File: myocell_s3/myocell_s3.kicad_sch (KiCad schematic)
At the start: 6 parts, among them J1 Conn_01x08, J2 Conn_01x08, J3 Conn_01x08, J4 Conn_01x08, J5 Battery Connector JC2, J6 USB_B_Micro

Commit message: recovery commit
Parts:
- removed J6: USB_B_Micro, Connector_USB:USB_Micro-B_Molex_47346-0001, symbol Connector:USB_B_Micro
- added J7: USB_C_Receptacle_USB2.0_16P, Connector_USB:USB_C_Receptacle_GCT_USB4110, symbol Connector:USB_C_Receptacle_USB2.0_16P
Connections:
- new net: J7.A1 (GND), J7.A12 (GND), J7.B1 (GND), J7.B12 (GND)
- new net: J7.A4 (VBUS), J7.A9 (VBUS), J7.B4 (VBUS), J7.B9 (VBUS)
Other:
- sheet cpu_wroom_esp32 ports: added none; removed EN

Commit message: working on schematic
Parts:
- added R14, R15: 5.1k, Resistor_SMD:R_0805_2012Metric_Pad1.20x1.40mm_HandSolder, symbol Device:R_US
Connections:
- net GND: now also R14.1, R15.1
- net power_supply/VUSB/2.1A: now also J7.A4 (VBUS), J7.A9 (VBUS), J7.B4 (VBUS), J7.B9 (VBUS)
- net at J7.A5 (CC1): now also R15.2
- net cpu_wroom_esp32/D+: now reaches J7.A6 (D+)
- net cpu_wroom_esp32/D+: now also J7.B6 (D+)
- net cpu_wroom_esp32/D-: now reaches J7.A7 (D-)
- net cpu_wroom_esp32/D-: now also J7.B7 (D-)
- net at J7.B5 (CC2): now also R14.2
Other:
- removed sheet usb
- sheet adc_8 ports: added RLD; removed adcVref, rld_Out
- sheet cpu_wroom_esp32 ports: added D+, D-; removed IO0, RXD0, TXD0
- moved on the sheet: J7

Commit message: working on schematic
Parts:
- added C55, C56: 10pF, Capacitor_SMD:C_0805_2012Metric_Pad1.18x1.45mm_HandSolder, symbol Device:C
- added R30, R31: 20, Resistor_SMD:R_0805_2012Metric_Pad1.20x1.40mm_HandSolder, symbol Device:R_US
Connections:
- net GND: now also C55.1, C56.2
- net cpu_wroom_esp32/D+: now also R30.1; no longer J7.A6 (D+), J7.B6 (D+)
- net cpu_wroom_esp32/D-: now also R31.1; no longer J7.A7 (D-), J7.B7 (D-)
- new net: C55.2, J7.A6 (D+), J7.B6 (D+), R30.2
- new net: C56.1, J7.A7 (D-), J7.B7 (D-), R31.2
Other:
- sheet cpu_wroom_esp32 ports: added clk, fspi_clk, fspi_cs0, fspi_miso, fspi_mosi, pwdn, reset, start; removed gpio18_vspi_sck, gpio19_vspi_miso, gpio21_start, gpio22_pwdn, gpio23_vspi_mosi, gpio27, gpio32, gpio33, gpio4, gpio5_vspi_ss
- note added: "esp32-s3 is spi master miso - master in, slave out mosi - master out, slave in"

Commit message: working on schematic transfer
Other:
- sheet cpu_wroom_esp32 ports: added bat_mon; removed none
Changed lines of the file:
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@@
 	(wire
 		(pts
+			(xy 151.13 101.6) (xy 189.23 101.6)
+		)
+		(stroke
+			(width 0)
+			(type default)
+		)
+	)
+	(wire
+		(pts
 			(xy 114.3 39.37) (xy 114.3 43.18)
 		)
@@
 	(wire
 		(pts
-			(xy 160.02 101.6) (xy 189.23 101.6)
-		)
-		(stroke
-			(width 0)
-			(type default)
-		)
-	)
-	(wire
-		(pts
 			(xy 86.36 62.23) (xy 90.17 62.23)
 		)
@@
 	(wire
 		(pts
+			(xy 151.13 101.6) (xy 151.13 72.39)
+		)
+		(stroke
+			(width 0)
+			(type default)
+		)
+	)
+	(wire
+		(pts
 			(xy 125.73 54.61) (xy 138.43 54.61)
 		)
@@
 			(effects
 				(font
+					(size 1.27 1.27)
+				)
+				(justify left)
+			)
+		)
+		(pin "bat_mon" input
+			(at 151.13 72.39 270)
+			(effects
+				(font

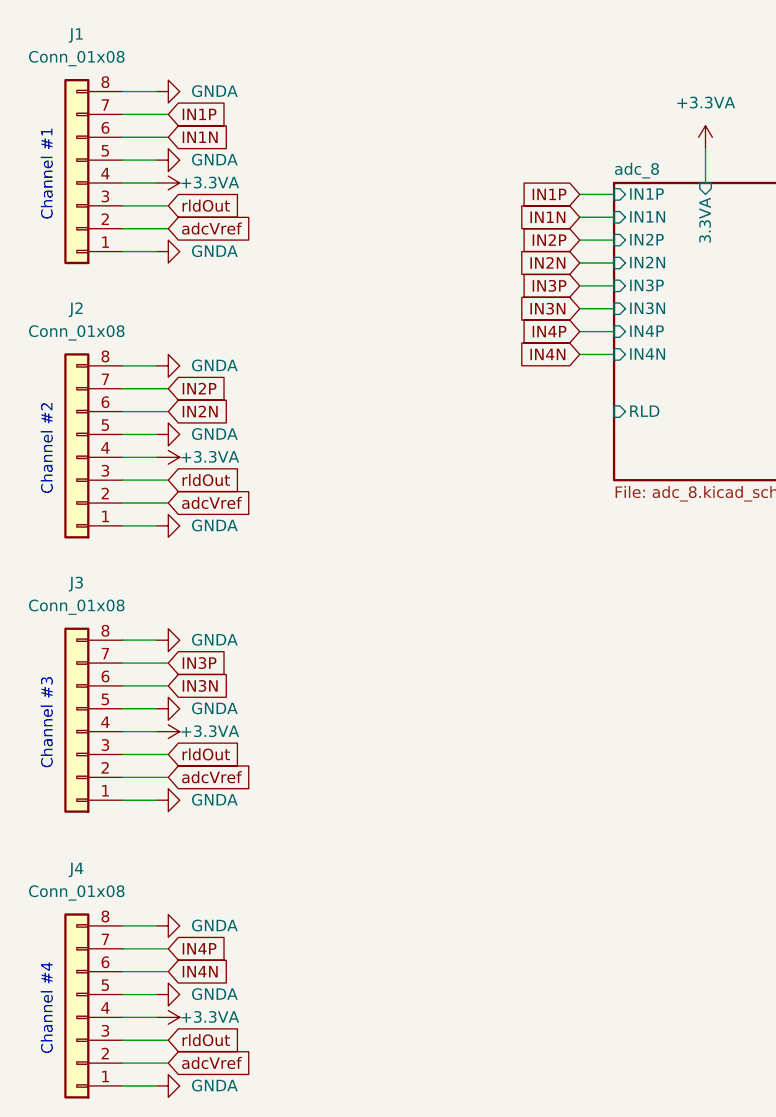
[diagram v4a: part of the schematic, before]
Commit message: RLDINV still unconnected
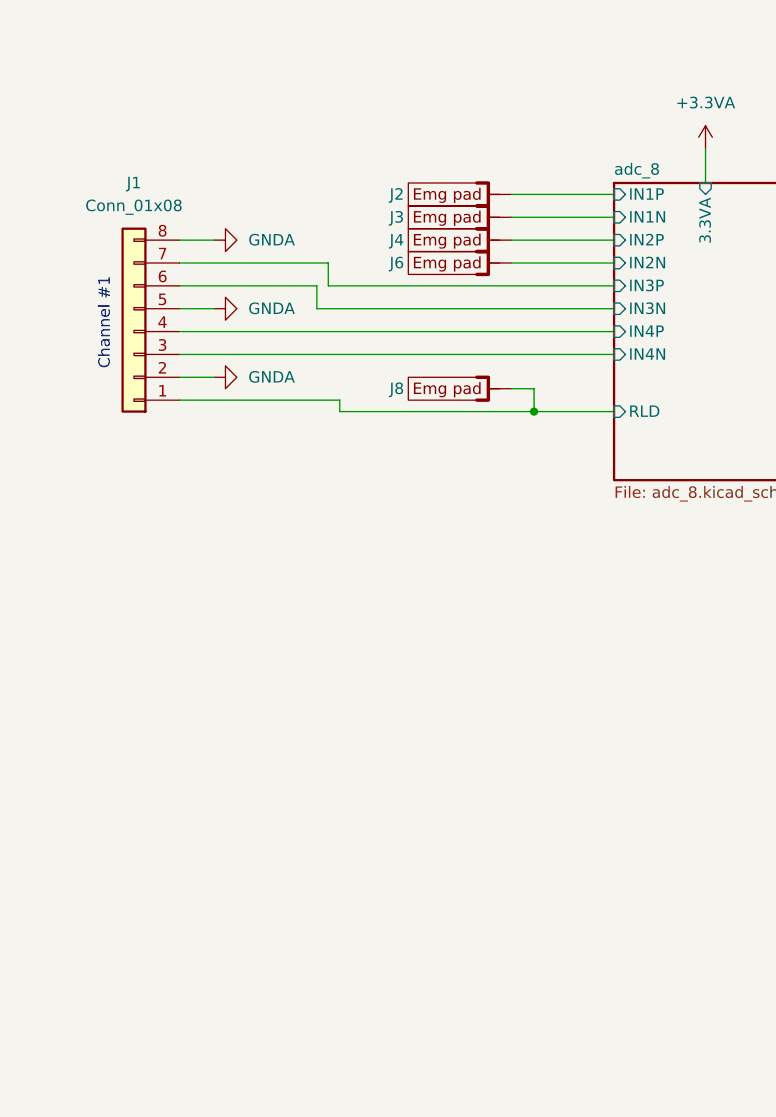
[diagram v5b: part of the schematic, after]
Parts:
- removed J2, J3, J4: Conn_01x08, Connector_FFC-FPC:Hirose_FH12-8S-0.5SH_1x08-1MP_P0.50mm_Horizontal, symbol Connector_Generic:Conn_01x08
- added J2, J3: (no value), emg:EMG_PAD_10_7, symbol myocell_s3:emg_pad
- added J4, J6, J8: ~, emg:EMG_PAD_10_7, symbol myocell_s3:emg_pad
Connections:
- net adcVref is gone; now on net GNDA: J1.2 (Pin_2)
- net +3.3VA: no longer J1.4 (Pin_4)
- net GNDA: no longer J1.1 (Pin_1)
- net adc_8/RLD: now also J1.1 (Pin_1), J8.1
- net IN1N renamed adc_8/IN3N
- net IN1P renamed adc_8/IN3P
- net rldOut renamed adc_8/IN4N
- new net adc_8/IN1N: J3.1
- new net adc_8/IN1P: J2.1
- new net adc_8/IN2N: J6.1
- new net adc_8/IN2P: J4.1
- new net adc_8/IN4P: J1.4 (Pin_4)
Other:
- note removed: "Channel #2"
- note removed: "Channel #3"
- note removed: "Channel #4"
- moved on the sheet: J1

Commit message: MSS22D18 slider switch added
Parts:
- J2, J3: value (none) -> ~
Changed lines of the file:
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@@
 			)
 		)
-		(property "Value" ""
+		(property "Value" "~"
 			(at 72.39 40.64 0)
 			(effects
@@
 			)
 		)
-		(property "Value" ""
+		(property "Value" "~"
 			(at 72.39 43.18 0)
 			(effects

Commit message: schematic and footprints done
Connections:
- net +3.3VA: now also J1.5 (Pin_5)
- net GNDA: no longer J1.5 (Pin_5)
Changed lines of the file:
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@@
+	(wire
+		(pts
+			(xy 41.91 57.15) (xy 44.45 57.15)
+		)
+		(stroke
+			(width 0)
+			(type default)
+		)
+	)
 	(wire
 		(pts
@@
 	(wire
 		(pts
-			(xy 41.91 57.15) (xy 45.72 57.15)
-		)
-		(stroke
-			(width 0)
-			(type default)
-		)
-	)
-	(wire
-		(pts
 			(xy 41.91 62.23) (xy 90.17 62.23)
 		)
@@
 			(width 0)
 			(type default)
+		)
+	)
+	(symbol
+		(lib_id "power:+3.3VA")
+		(at 44.45 57.15 270)
+		(unit 1)
+		(exclude_from_sim no)
+		(in_bom yes)
+		(on_board yes)
+		(dnp no)
+		(property "Reference" "#PWR02"
+			(at 40.64 57.15 0)
+			(effects
+				(font
+					(size 1.27 1.27)
+				)
+				(hide yes)
+			)
+		)
+		(property "Value" "+3.3VA"
+			(at 47.498 57.15 90)
+			(effects
+				(font
+					(size 1.27 1.27)
+				)
+				(justify left)
+			)
+		)
+		(property "Footprint" ""
+			(at 44.45 57.15 0)
+			(effects
+				(font
+					(size 1.27 1.27)
+				)
+				(hide yes)
+			)
+		)
+		(property "Datasheet" ""
+			(at 44.45 57.15 0)
+			(effects
+				(font
+					(size 1.27 1.27)
+				)
+				(hide yes)
+			)
+		)
+		(property "Description" "Power symbol creates a global label with name \"+3.3VA\""
+			(at 44.45 57.15 0)
+			(effects
+				(font
+					(size 1.27 1.27)
+				)
+				(hide yes)
+			)
+		)
+		(pin "1"
+		)
+		(instances
+			(project "myocell_s3"
+				(path "/871ff10b-bde5-471c-b91a-de58aa271388"
+					(reference "#PWR02")
+					(unit 1)
+				)
+			)
 		)
 	)
@@
 					(unit 1)
 				)
-			)
-		)
-	)
-	(symbol
-		(lib_id "power:GNDA")
-		(at 45.72 57.15 90)
-		(unit 1)
-		(exclude_from_sim no)
-		(in_bom yes)
-		(on_board yes)
-		(dnp no)
-		(fields_autoplaced yes)
-		(property "Reference" "#PWR02"
-			(at 52.07 57.15 0)
-			(effects
-				(font
-					(size 1.27 1.27)
-				)
-				(hide yes)
-			)
-		)
-		(property "Value" "GNDA"
-			(at 49.53 57.1499 90)
-			(effects
-				(font
-					(size 1.27 1.27)
-				)
-				(justify right)
-			)
-		)
-		(property "Footprint" ""
-			(at 45.72 57.15 0)
-			(effects
-				(font
-					(size 1.27 1.27)
-				)
-				(hide yes)
-			)
-		)
-		(property "Datasheet" ""
-			(at 45.72 57.15 0)
-			(effects
-				(font
-					(size 1.27 1.27)
-				)
-				(hide yes)
-			)
-		)
-		(property "Description" "Power symbol creates a global label with name \"GNDA\" , analog ground"
-			(at 45.72 57.15 0)
-			(effects
-				(font
-					(size 1.27 1.27)
-				)
-				(hide yes)
-			)
-		)
-		(pin "1"
-		)
-		(instances
-			(project "myocell_s3"
-				(path "/871ff10b-bde5-471c-b91a-de58aa271388"
-					(reference "#PWR02")
-					(unit 1)
-				)

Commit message: working on component placement
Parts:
- J2, J3, J4, J6, J8: value ~ -> (none)
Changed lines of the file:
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@@
 			)
 		)
-		(property "Value" "~"
+		(property "Value" ""
 			(at 72.39 45.72 0)
 			(effects
@@
 			)
 		)
-		(property "Value" "~"
+		(property "Value" ""
 			(at 72.39 40.64 0)
 			(effects
@@
 			)
 		)
-		(property "Value" "~"
+		(property "Value" ""
 			(at 72.39 48.26 0)
 			(effects
@@
 			)
 		)
-		(property "Value" "~"
+		(property "Value" ""
 			(at 72.39 62.23 0)
 			(effects
@@
 			)
 		)
-		(property "Value" "~"
+		(property "Value" ""
 			(at 72.39 43.18 0)
 			(effects
